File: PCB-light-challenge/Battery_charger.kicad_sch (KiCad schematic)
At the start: 5 parts

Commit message: Footprint van de eds protection device aangepast naar sod 523
https://nl.farnell.com/en-NL/rohm/rsb6-8smt2n/esd-protection-diode-sod-523-2/dp/2914120
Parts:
- D1: footprint Diode_SMD:D_SOD-323_HandSoldering -> Diode_SMD:D_SOD-523
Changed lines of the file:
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@@
       (effects (font (size 1.27 1.27)) (justify right) hide)
     )
-    (property "Footprint" "Diode_SMD:D_SOD-323_HandSoldering" (at 100.33 59.055 0)
+    (property "Footprint" "Diode_SMD:D_SOD-523" (at 100.33 59.055 0)
       (effects (font (size 1.27 1.27)) hide)
     )

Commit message: EDS device bij 230 verwijdert
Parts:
- removed D1: ESD9B3.3ST5G, Diode_SMD:D_SOD-523, symbol Diode:ESD9B3.3ST5G
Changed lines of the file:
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@@
   (junction (at 57.658 57.785) (diameter 0) (color 0 0 0 0)
-  )
-  (junction (at 100.33 64.135) (diameter 0) (color 0 0 0 0)
   )
   (junction (at 45.847 57.785) (diameter 0) (color 0 0 0 0)
   )
   (junction (at 102.743 53.975) (diameter 0) (color 0 0 0 0)
-  )
-  (junction (at 100.33 53.975) (diameter 0) (color 0 0 0 0)
   )
   (wire (pts (xy 137.795 62.23) (xy 143.51 62.23))
@@
   )
   (wire (pts (xy 105.41 60.96) (xy 105.41 64.135))
-    (stroke (width 0) (type default))
-  )
-  (wire (pts (xy 100.33 53.975) (xy 100.33 55.245))
     (stroke (width 0) (type default))
   )
@@
     (stroke (width 0) (type default))
   )
-  (wire (pts (xy 94.107 64.135) (xy 100.33 64.135))
+  (wire (pts (xy 94.107 64.135) (xy 105.41 64.135))
     (stroke (width 0) (type default))
   )
@@
     (stroke (width 0) (type default))
   )
-  (wire (pts (xy 100.33 62.865) (xy 100.33 64.135))
-    (stroke (width 0) (type default))
-  )
   (wire (pts (xy 45.847 55.499) (xy 45.847 57.785))
-    (stroke (width 0) (type default))
-  )
-  (wire (pts (xy 100.33 64.135) (xy 105.41 64.135))
     (stroke (width 0) (type default))
   )
@@
     (stroke (width 0) (type default))
   )
-  (wire (pts (xy 92.075 53.975) (xy 100.33 53.975))
+  (wire (pts (xy 92.075 53.975) (xy 102.743 53.975))
     (stroke (width 0) (type default))
   )
@@
   )
   (wire (pts (xy 137.795 66.04) (xy 143.51 66.04))
-    (stroke (width 0) (type default))
-  )
-  (wire (pts (xy 100.33 53.975) (xy 102.743 53.975))
     (stroke (width 0) (type default))
   )
@@
     )
   )
-  (symbol (lib_id "Diode:ESD9B3.3ST5G") (at 100.33 59.055 90) (unit 1)
-    (in_bom yes) (on_board yes) (dnp no)
-    (property "Reference" "D1" (at 102.235 59.055 90)
-      (effects (font (size 1.27 1.27)) (justify right))
-    )
-    (property "Value" "ESD9B3.3ST5G" (at 103.505 60.325 90)
-      (effects (font (size 1.27 1.27)) (justify right) hide)
-    )
-    (property "Footprint" "Diode_SMD:D_SOD-523" (at 100.33 59.055 0)
-      (effects (font (size 1.27 1.27)) hide)
-    )
-    (property "Datasheet" "https://www.onsemi.com/pub/Collateral/ESD9B-D.PDF" (at 100.33 59.055 0)
-      (effects (font (size 1.27 1.27)) hide)
-    )
-    (pin "1")
-    (pin "2")
-    (instances
-      (project "PCB-light-challenge"
-        (path "/35573e8f-7834-430c-81d2-239f316c7834/1ee2b17a-9b36-4608-9d61-b871128bc979"
-          (reference "D1") (unit 1)
-        )
-      )
-    )
-  )

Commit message: eds terug gezet
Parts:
- added D1: ESD9B3.3ST5G, Diode_SMD:D_SOD-523, symbol Diode:ESD9B3.3ST5G
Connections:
- net +5V: now also D1.2 (A2)
- net at PS1.4 (-VOUT), U1.5 (IN-): now also D1.1 (A1)
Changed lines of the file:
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@@
   (junction (at 57.658 57.785) (diameter 0) (color 0 0 0 0)
   )
+  (junction (at 99.695 64.135) (diameter 0) (color 0 0 0 0)
+  )
   (junction (at 45.847 57.785) (diameter 0) (color 0 0 0 0)
+  )
+  (junction (at 99.695 53.975) (diameter 0) (color 0 0 0 0)
   )
   (junction (at 102.743 53.975) (diameter 0) (color 0 0 0 0)
   )
   (wire (pts (xy 137.795 62.23) (xy 143.51 62.23))
+    (stroke (width 0) (type default))
+  )
+  (wire (pts (xy 99.695 62.865) (xy 99.695 64.135))
     (stroke (width 0) (type default))
   )
@@
     (stroke (width 0) (type default))
   )
-  (wire (pts (xy 94.107 64.135) (xy 105.41 64.135))
+  (wire (pts (xy 94.107 64.135) (xy 99.695 64.135))
     (stroke (width 0) (type default))
   )
@@
     (stroke (width 0) (type default))
   )
-  (wire (pts (xy 92.075 53.975) (xy 102.743 53.975))
+  (wire (pts (xy 92.075 53.975) (xy 99.695 53.975))
     (stroke (width 0) (type default))
   )
@@
   )
   (wire (pts (xy 109.855 60.96) (xy 105.41 60.96))
+    (stroke (width 0) (type default))
+  )
+  (wire (pts (xy 99.695 64.135) (xy 105.41 64.135))
+    (stroke (width 0) (type default))
+  )
+  (wire (pts (xy 99.695 53.975) (xy 102.743 53.975))
+    (stroke (width 0) (type default))
+  )
+  (wire (pts (xy 99.695 53.975) (xy 99.695 55.245))
     (stroke (width 0) (type default))
   )
@@
     )
   )
+  (symbol (lib_id "Diode:ESD9B3.3ST5G") (at 99.695 59.055 90) (unit 1)
+    (in_bom yes) (on_board yes) (dnp no)
+    (property "Reference" "D1" (at 98.425 65.405 90)
+      (effects (font (size 1.27 1.27)) (justify right))
+    )
+    (property "Value" "ESD9B3.3ST5G" (at 102.87 60.325 90)
+      (effects (font (size 1.27 1.27)) (justify right) hide)
+    )
+    (property "Footprint" "Diode_SMD:D_SOD-523" (at 99.695 59.055 0)
+      (effects (font (size 1.27 1.27)) hide)
+    )
+    (property "Datasheet" "https://www.onsemi.com/pub/Collateral/ESD9B-D.PDF" (at 99.695 59.055 0)
+      (effects (font (size 1.27 1.27)) hide)
+    )
+    (pin "1")
+    (pin "2")
+    (instances
+      (project "PCB-light-challenge"
+        (path "/35573e8f-7834-430c-81d2-239f316c7834/1ee2b17a-9b36-4608-9d61-b871128bc979"
+          (reference "D1") (unit 1)
+        )
+        (path "/35573e8f-7834-430c-81d2-239f316c7834/a8982b6c-f9f4-4ae9-b882-3fbabc855f32"
+          (reference "D2") (unit 1)
+        )
+      )
+    )
+  )

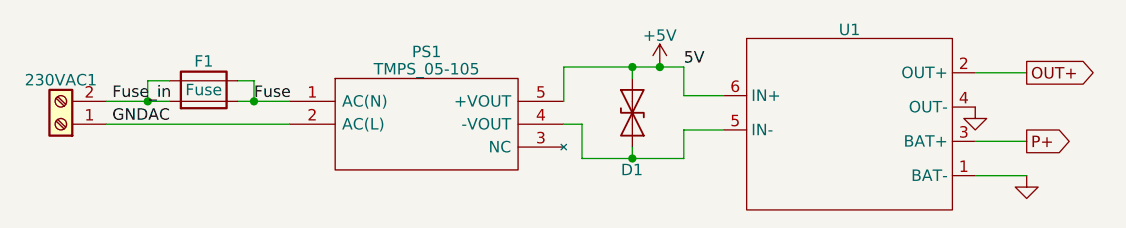
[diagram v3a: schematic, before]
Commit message: TP footprint verandert,  apparte grond (P-) gemaakt.  AC  clearance verandert.  connector voor PIR verandert
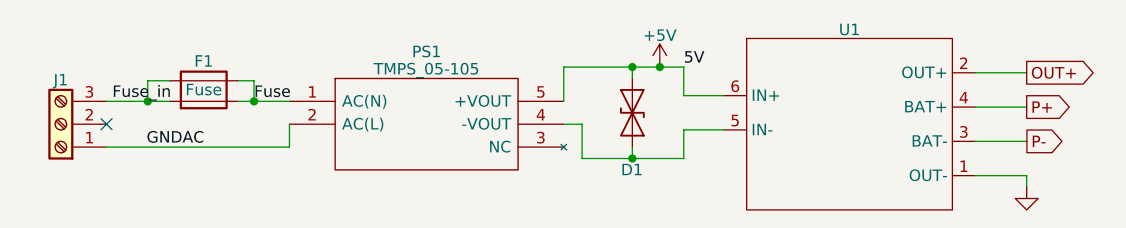
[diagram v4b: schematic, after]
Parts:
- removed 230VAC1: Screw_Terminal_01x02, TerminalBlock_TE-Connectivity:TerminalBlock_TE_282834-2_1x02_P2.54mm_Horizontal, symbol Connector:Screw_Terminal_01x02
- added J1: Screw_Terminal_01x03, TerminalBlock:TerminalBlock_bornier-3_P5.08mm, symbol Connector:Screw_Terminal_01x03
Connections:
- net Fuse_in: now also J1.3 (Pin_3)
- net GND: no longer U1.4 (OUT-)
- net GNDAC: now also J1.1 (Pin_1)
- net P+: now also U1.4 (BAT+); no longer U1.3 (BAT+)
- new net P-: U1.3 (BAT-)
- no-connect marks 0 -> 1
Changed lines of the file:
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@@
   (junction (at 102.743 53.975) (diameter 0) (color 0 0 0 0)
   )
-  (wire (pts (xy 137.795 62.23) (xy 143.51 62.23))
+  (no_connect (at 41.275 60.325))
+  (wire (pts (xy 137.795 62.23) (xy 143.5354 62.23))
     (stroke (width 0) (type default))
   )
@@
     (stroke (width 0) (type default))
   )
-  (wire (pts (xy 41.275 60.325) (xy 61.595 60.325))
-    (stroke (width 0) (type default))
-  )
   (wire (pts (xy 102.743 53.975) (xy 105.41 53.975))
     (stroke (width 0) (type default))
   )
+  (wire (pts (xy 41.275 62.865) (xy 61.595 62.865))
+    (stroke (width 0) (type default))
+  )
   (wire (pts (xy 55.88 57.785) (xy 57.658 57.785))
     (stroke (width 0) (type default))
@@
     (stroke (width 0) (type default))
   )
+  (wire (pts (xy 137.795 58.42) (xy 143.51 58.42))
+    (stroke (width 0) (type default))
+  )
   (wire (pts (xy 45.847 55.499) (xy 45.847 57.785))
     (stroke (width 0) (type default))
@@
   )
   (wire (pts (xy 109.855 60.96) (xy 105.41 60.96))
+    (stroke (width 0) (type default))
+  )
+  (wire (pts (xy 61.595 62.865) (xy 61.595 60.325))
+    (stroke (width 0) (type default))
+  )
+  (wire (pts (xy 143.51 66.04) (xy 143.51 67.31))
     (stroke (width 0) (type default))
   )
@@
     (effects (font (size 1.27 1.27)) (justify left bottom))
   )
-  (label "GNDAC" (at 41.91 60.325 0) (fields_autoplaced)
+  (label "GNDAC" (at 45.72 62.865 0) (fields_autoplaced)
     (effects (font (size 1.27 1.27)) (justify left bottom))
   )
@@
     (effects (font (size 1.27 1.27)) (justify left bottom))
   )
-  (global_label "P+" (shape output) (at 143.51 62.23 0) (fields_autoplaced)
+  (global_label "P-" (shape output) (at 143.5354 62.23 0) (fields_autoplaced)
     (effects (font (size 1.27 1.27)) (justify left))
-    (property "Intersheetrefs" "${INTERSHEET_REFS}" (at 149.2582 62.23 0)
+    (property "Intersheetrefs" "${INTERSHEET_REFS}" (at 149.2836 62.23 0)
+      (effects (font (size 1.27 1.27)) (justify left) hide)
+    )
+  )
+  (global_label "P+" (shape output) (at 143.51 58.42 0) (fields_autoplaced)
+    (effects (font (size 1.27 1.27)) (justify left))
+    (property "Intersheetrefs" "${INTERSHEET_REFS}" (at 149.2582 58.42 0)
       (effects (font (size 1.27 1.27)) (justify left) hide)
     )
@@
         (path "/35573e8f-7834-430c-81d2-239f316c7834/a8982b6c-f9f4-4ae9-b882-3fbabc855f32"
           (reference "D2") (unit 1)
-        )
-      )
-    )
-  )
-  (symbol (lib_id "Connector:Screw_Terminal_01x02") (at 36.195 60.325 180) (unit 1)
-    (in_bom yes) (on_board yes) (dnp no) (fields_autoplaced)
-    (property "Reference" "230VAC1" (at 36.195 55.4261 0)
-      (effects (font (size 1.27 1.27)))
-    )
-    (property "Value" "Screw_Terminal_01x02" (at 36.195 55.4261 0)
-      (effects (font (size 1.27 1.27)) hide)
-    )
-    (property "Footprint" "TerminalBlock_TE-Connectivity:TerminalBlock_TE_282834-2_1x02_P2.54mm_Horizontal" (at 36.195 60.325 0)
-      (effects (font (size 1.27 1.27)) hide)
-    )
-    (property "Datasheet" "~" (at 36.195 60.325 0)
-      (effects (font (size 1.27 1.27)) hide)
-    )
-    (pin "1")
-    (pin "2")
-    (instances
-      (project "PCB-light-challenge"
-        (path "/35573e8f-7834-430c-81d2-239f316c7834/1ee2b17a-9b36-4608-9d61-b871128bc979"
-          (reference "230VAC1") (unit 1)
         )
       )
@@
     )
   )
-  (symbol (lib_id "power:GND") (at 137.795 58.42 0) (unit 1)
-    (in_bom yes) (on_board yes) (dnp no) (fields_autoplaced)
-    (property "Reference" "#PWR019" (at 137.795 64.77 0)
-      (effects (font (size 1.27 1.27)) hide)
-    )
-    (property "Value" "GND" (at 137.795 62.5555 0)
-      (effects (font (size 1.27 1.27)) hide)
-    )
-    (property "Footprint" "" (at 137.795 58.42 0)
-      (effects (font (size 1.27 1.27)) hide)
-    )
-    (property "Datasheet" "" (at 137.795 58.42 0)
+  (symbol (lib_id "Connector:Screw_Terminal_01x03") (at 36.195 60.325 180) (unit 1)
+    (in_bom yes) (on_board yes) (dnp no) (fields_autoplaced)
+    (property "Reference" "J1" (at 36.195 55.4261 0)
+      (effects (font (size 1.27 1.27)))
+    )
+    (property "Value" "Screw_Terminal_01x03" (at 36.195 55.4261 0)
+      (effects (font (size 1.27 1.27)) hide)
+    )
+    (property "Footprint" "TerminalBlock:TerminalBlock_bornier-3_P5.08mm" (at 36.195 60.325 0)
+      (effects (font (size 1.27 1.27)) hide)
+    )
+    (property "Datasheet" "~" (at 36.195 60.325 0)
+      (effects (font (size 1.27 1.27)) hide)
+    )
+    (pin "1")
+    (pin "2")
+    (pin "3")
+    (instances
+      (project "PCB-light-challenge"
+        (path "/35573e8f-7834-430c-81d2-239f316c7834/1ee2b17a-9b36-4608-9d61-b871128bc979"
+          (reference "J1") (unit 1)
+        )
+      )
+    )
+  )
+  (symbol (lib_id "power:GND") (at 143.51 67.31 0) (unit 1)
+    (in_bom yes) (on_board yes) (dnp no) (fields_autoplaced)
+    (property "Reference" "#PWR019" (at 143.51 73.66 0)
+      (effects (font (size 1.27 1.27)) hide)
+    )
+    (property "Value" "GND" (at 143.51 71.4455 0)
+      (effects (font (size 1.27 1.27)) hide)
+    )
+    (property "Footprint" "" (at 143.51 67.31 0)
+      (effects (font (size 1.27 1.27)) hide)
+    )
+    (property "Datasheet" "" (at 143.51 67.31 0)
       (effects (font (size 1.27 1.27)) hide)
     )
@@
         )
       )
-    )
-  )
-  (symbol (lib_id "power:GND") (at 143.51 66.04 0) (unit 1)
-    (in_bom yes) (on_board yes) (dnp no) (fields_autoplaced)
-    (property "Reference" "#PWR024" (at 143.51 72.39 0)
-      (effects (font (size 1.27 1.27)) hide)
-    )
-    (property "Value" "GND" (at 143.51 70.1755 0)
-      (effects (font (size 1.27 1.27)) hide)
-    )
-    (property "Footprint" "" (at 143.51 66.04 0)
-      (effects (font (size 1.27 1.27)) hide)
-    )
-    (property "Datasheet" "" (at 143.51 66.04 0)
-      (effects (font (size 1.27 1.27)) hide)
-    )
-    (pin "1")
-    (instances
-      (project "PCB-light-challenge"
-        (path "/35573e8f-7834-430c-81d2-239f316c7834/1ee2b17a-9b36-4608-9d61-b871128bc979"
-          (reference "#PWR024") (unit 1)
-        )
-      )

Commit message: Vias  kleiner gemaakt en grond GND genoemd op silkscreen
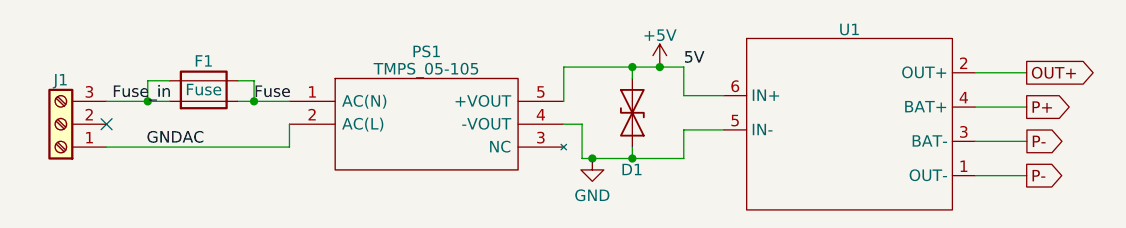
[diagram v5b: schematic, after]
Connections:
- net GND: now also D1.1 (A1), PS1.4 (-VOUT), U1.5 (IN-); no longer U1.1 (OUT-)
- net P-: now also U1.1 (OUT-)
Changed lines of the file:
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@@
   (junction (at 45.847 57.785) (diameter 0) (color 0 0 0 0)
+  )
+  (junction (at 95.25 64.135) (diameter 0) (color 0 0 0 0)
   )
   (junction (at 99.695 53.975) (diameter 0) (color 0 0 0 0)
@@
     (stroke (width 0) (type default))
   )
+  (wire (pts (xy 95.25 64.135) (xy 99.695 64.135))
+    (stroke (width 0) (type default))
+  )
   (wire (pts (xy 55.88 57.785) (xy 57.658 57.785))
     (stroke (width 0) (type default))
@@
     (stroke (width 0) (type default))
   )
-  (wire (pts (xy 94.107 64.135) (xy 99.695 64.135))
+  (wire (pts (xy 94.107 64.135) (xy 95.25 64.135))
     (stroke (width 0) (type default))
   )
@@
   )
   (wire (pts (xy 61.595 62.865) (xy 61.595 60.325))
-    (stroke (width 0) (type default))
-  )
-  (wire (pts (xy 143.51 66.04) (xy 143.51 67.31))
     (stroke (width 0) (type default))
   )
@@
     (effects (font (size 1.27 1.27)) (justify left))
     (property "Intersheetrefs" "${INTERSHEET_REFS}" (at 149.2582 58.42 0)
+      (effects (font (size 1.27 1.27)) (justify left) hide)
+    )
+  )
+  (global_label "P-" (shape output) (at 143.51 66.04 0) (fields_autoplaced)
+    (effects (font (size 1.27 1.27)) (justify left))
+    (property "Intersheetrefs" "${INTERSHEET_REFS}" (at 149.2582 66.04 0)
       (effects (font (size 1.27 1.27)) (justify left) hide)
     )
@@
         (path "/35573e8f-7834-430c-81d2-239f316c7834/1ee2b17a-9b36-4608-9d61-b871128bc979"
           (reference "PS1") (unit 1)
+        )
+      )
+    )
+  )
+  (symbol (lib_id "power:GND") (at 95.25 64.135 0) (unit 1)
+    (in_bom yes) (on_board yes) (dnp no) (fields_autoplaced)
+    (property "Reference" "#PWR01" (at 95.25 70.485 0)
+      (effects (font (size 1.27 1.27)) hide)
+    )
+    (property "Value" "GND" (at 95.25 68.2705 0)
+      (effects (font (size 1.27 1.27)))
+    )
+    (property "Footprint" "" (at 95.25 64.135 0)
+      (effects (font (size 1.27 1.27)) hide)
+    )
+    (property "Datasheet" "" (at 95.25 64.135 0)
+      (effects (font (size 1.27 1.27)) hide)
+    )
+    (pin "1")
+    (instances
+      (project "PCB-light-challenge"
+        (path "/35573e8f-7834-430c-81d2-239f316c7834/1ee2b17a-9b36-4608-9d61-b871128bc979"
+          (reference "#PWR01") (unit 1)
         )
       )
@@
         )
       )
-    )
-  )
-  (symbol (lib_id "power:GND") (at 143.51 67.31 0) (unit 1)
-    (in_bom yes) (on_board yes) (dnp no) (fields_autoplaced)
-    (property "Reference" "#PWR019" (at 143.51 73.66 0)
-      (effects (font (size 1.27 1.27)) hide)
-    )
-    (property "Value" "GND" (at 143.51 71.4455 0)
-      (effects (font (size 1.27 1.27)) hide)
-    )
-    (property "Footprint" "" (at 143.51 67.31 0)
-      (effects (font (size 1.27 1.27)) hide)
-    )
-    (property "Datasheet" "" (at 143.51 67.31 0)
-      (effects (font (size 1.27 1.27)) hide)
-    )
-    (pin "1")
-    (instances
-      (project "PCB-light-challenge"
-        (path "/35573e8f-7834-430c-81d2-239f316c7834/1ee2b17a-9b36-4608-9d61-b871128bc979"
-          (reference "#PWR019") (unit 1)
-        )
-      )

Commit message: AC (L) en (N)  weer nagekeken en aangepast
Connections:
- net Fuse: now also PS1.2 (AC(L)); no longer PS1.1 (AC(N))
- net GNDAC: now also PS1.1 (AC(N)); no longer PS1.2 (AC(L))
